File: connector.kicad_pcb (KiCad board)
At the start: 2 copper layers, 26 x 9.7 mm, 3 parts, among them J4 BAT_OUTPUT, SW1 SW_Push

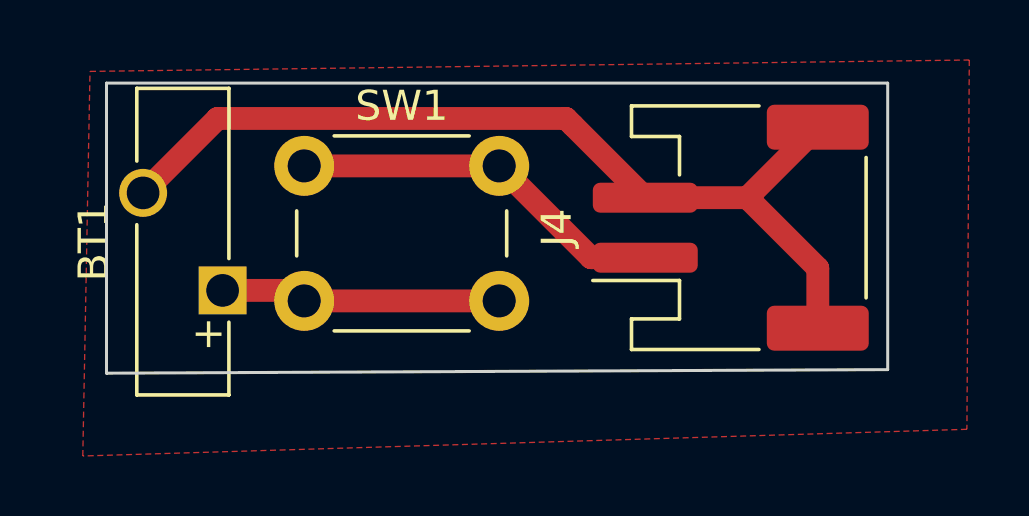
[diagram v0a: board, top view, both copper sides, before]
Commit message: feat: change the 2 pin connector from jst ph to jst xh
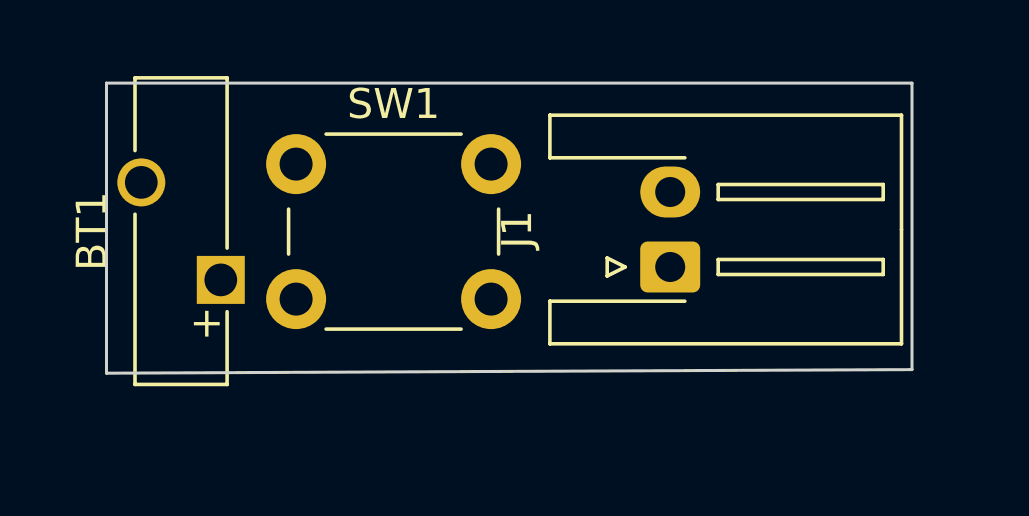
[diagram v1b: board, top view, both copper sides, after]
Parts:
- removed J4: BAT_OUTPUT, Connector_JST:JST_PH_S2B-PH-SM4-TB_1x02-1MP_P2.00mm_Horizontal
- added J1: Conn_01x02, Connector_JST:JST_XH_S2B-XH-A-1_1x02_P2.50mm_Horizontal, F.Cu at (167.9, 91.7)
- moved BT1 0.36 mm to (153.0, 92.1)
- moved SW1 0.28 mm to (155.5, 88.3)
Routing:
- net Net-(BT1-Pad2): track 30.9 -> 0.00 mm
- net Net-(J1-Pad2): track 12.6 -> 0.00 mm
- net Net-(BT1-Pad1): track 9.36 -> 0.00 mm
- removed copper zone on F.Cu, net Net-(BT1-Pad1)
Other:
- board size 26 x 9.7 mm -> 26.8 x 9.7 mm

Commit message: feat: update the jst package
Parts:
- J1: footprint Connector_JST:JST_XH_S2B-XH-A-1_1x02_P2.50mm_Horizontal -> keyboard:JST_XH_S2B-XH-A-1_1x02_P2.50mm_Horizontal
- moved J1 2.15 mm to (165.8, 91.5)
- moved SW1 0.52 mm to (155.9, 87.9)
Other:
- board size 26.8 x 9.7 mm -> 25.2 x 8.6 mm

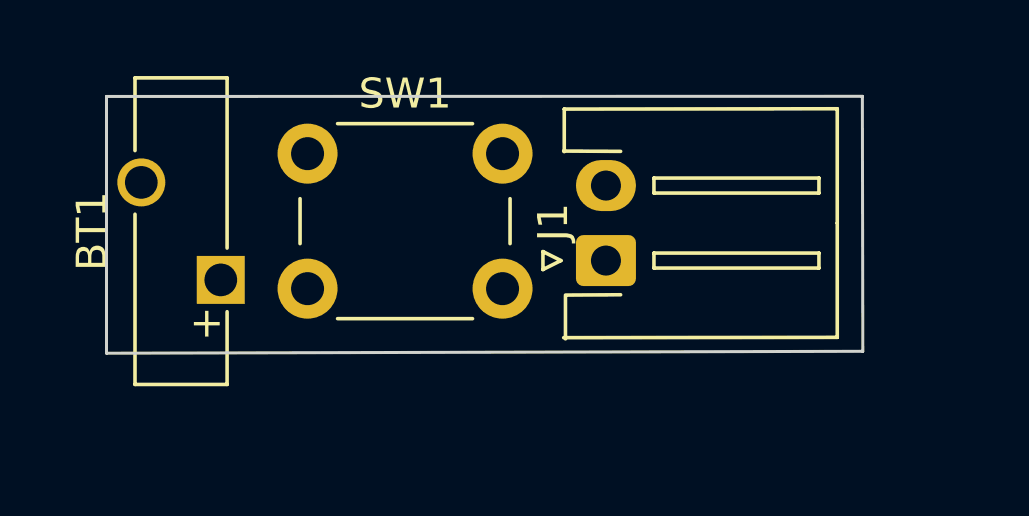
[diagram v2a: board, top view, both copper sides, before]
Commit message: feat: update differential skew
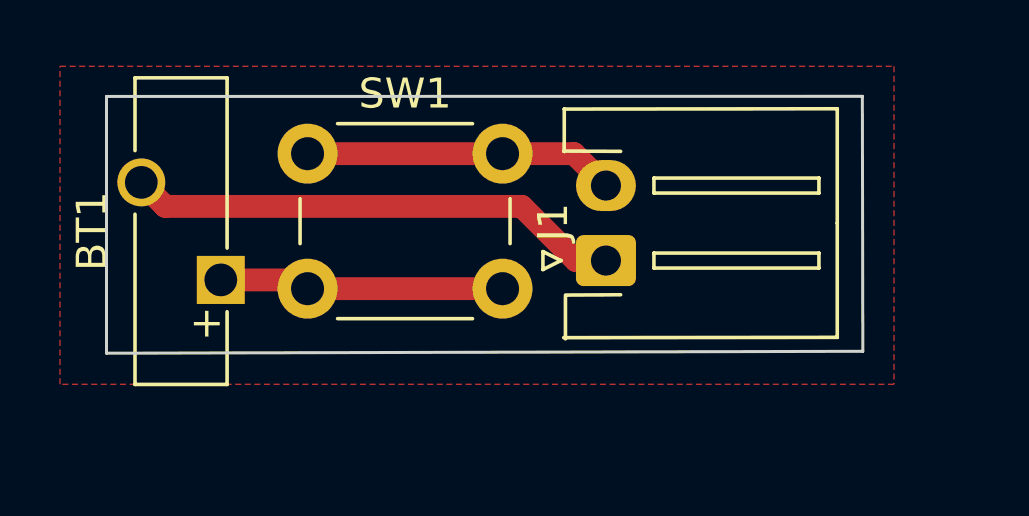
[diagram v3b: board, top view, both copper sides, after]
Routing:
- net Net-(BT1-Pad2): track 0.00 -> 16.6 mm
- net Net-(J1-Pad2): track 0.00 -> 10.4 mm
- net Net-(BT1-Pad1): track 0.00 -> 9.51 mm
- added copper zone on F.Cu, net Net-(BT1-Pad1)
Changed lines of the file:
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@@
-(kicad_pcb (version 20171130) (host pcbnew "(5.1.6-0-10_14)")
+(kicad_pcb (version 20171130) (host pcbnew "(5.1.5-0-10_14)")
   (general
     (thickness 1.6)
     (drawings 4)
-    (tracks 0)
+    (tracks 10)
     (zones 0)
     (modules 3)
@@
   )
   (setup
-    (last_trace_width 0.25)
+    (last_trace_width 0.762)
     (user_trace_width 0.762)
     (user_trace_width 1.524)
@@
   (gr_line (start 149.15 94.56422) (end 174.36084 94.5) (layer Edge.Cuts) (width 0.1))
   (gr_line (start 149.15 86.00518) (end 174.3456 86) (layer Edge.Cuts) (width 0.1))
+  (segment (start 151.109999 89.669999) (end 150.31 88.87) (width 0.762) (layer F.Cu) (net 1))
+  (segment (start 162.992939 89.669999) (end 151.109999 89.669999) (width 0.762) (layer F.Cu) (net 1))
+  (segment (start 164.7985 91.47556) (end 162.992939 89.669999) (width 0.762) (layer F.Cu) (net 1))
+  (segment (start 165.7985 91.47556) (end 164.7985 91.47556) (width 0.762) (layer F.Cu) (net 1))
+  (segment (start 155.55992 92.12) (end 155.85186 92.41194) (width 0.762) (layer F.Cu) (net 2))
+  (segment (start 152.96 92.12) (end 155.55992 92.12) (width 0.762) (layer F.Cu) (net 2))
+  (segment (start 155.85186 92.41194) (end 162.35186 92.41194) (width 0.762) (layer F.Cu) (net 2))
+  (segment (start 155.85186 87.91194) (end 162.35186 87.91194) (width 0.762) (layer F.Cu) (net 3))
+  (segment (start 164.73488 87.91194) (end 165.7985 88.97556) (width 0.762) (layer F.Cu) (net 3))
+  (segment (start 162.35186 87.91194) (end 164.73488 87.91194) (width 0.762) (layer F.Cu) (net 3))
+  (zone (net 2) (net_name "Net-(BT1-Pad1)") (layer F.Cu) (hatch edge 0.508)
+    (connect_pads (clearance 0.508))
+    (min_thickness 0.254)
+    (fill yes (arc_segments 32) (thermal_gap 0.508) (thermal_bridge_width 0.508))
+    (polygon
+      (pts
+        (xy 175.4 95.6) (xy 147.6 95.6) (xy 147.6 85) (xy 175.4 85)
+      )
+    )
+  )
 )
